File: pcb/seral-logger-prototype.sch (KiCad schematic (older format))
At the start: 51 parts, among them J1 Conn_ARM_JTAG_SWD_10, J2 Conn_01x04_Female, J3 Conn_01x04_Female, J4 Conn_01x03_Male, SW1 Rotary_Encoder_Switch_DualLED, SW2 SW_SPDT, U1 STM32G070KBT6, U2 74LVC3G17, U3 TLV70228_SOT23-5, U4 sn74lv1t34, U5 TLV61046ADB, U6 sn74lv1t34

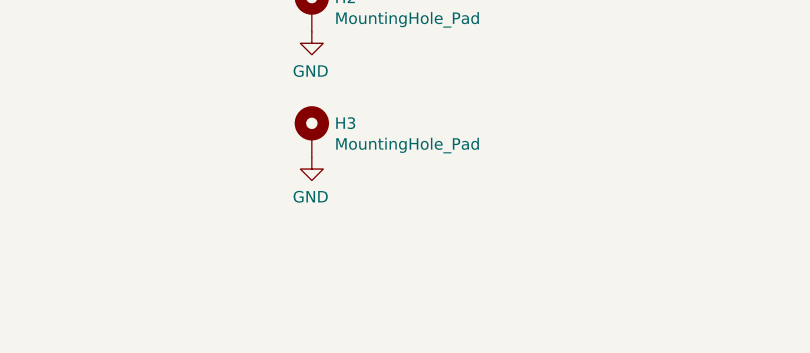
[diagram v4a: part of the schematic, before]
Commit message: Update slide switch placement and add mounting hole
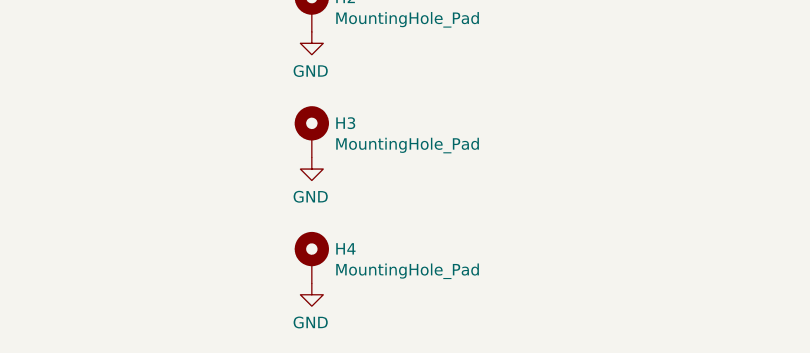
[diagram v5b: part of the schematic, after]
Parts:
- added H4: MountingHole_Pad, MountingHole:MountingHole_2.2mm_M2_Pad_Via, symbol Mechanical:MountingHole_Pad
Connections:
- net GND: now also H4.1
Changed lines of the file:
@@
 NoConn ~ 2850 2150
 NoConn ~ 2850 2250
+$Comp
+L Mechanical:MountingHole_Pad H4
+U 1 1 5E5755E9
+P 8450 8400
+F 0 "H4" H 8550 8449 50  0000 L CNN
+F 1 "MountingHole_Pad" H 8550 8358 50  0000 L CNN
+F 2 "MountingHole:MountingHole_2.2mm_M2_Pad_Via" H 8450 8400 50  0001 C CNN
+F 3 "~" H 8450 8400 50  0001 C CNN
+	1    8450 8400
+	1    0    0    -1
+$EndComp
+$Comp
+L power:GND #PWR?
+U 1 1 5E5755EF
+P 8450 8500
+F 0 "#PWR?" H 8450 8250 50  0001 C CNN
+F 1 "GND" H 8455 8327 50  0000 C CNN
+F 2 "" H 8450 8500 50  0001 C CNN
+F 3 "" H 8450 8500 50  0001 C CNN
+	1    8450 8500
+	-1   0    0    -1
+$EndComp
 $EndSCHEMATC
